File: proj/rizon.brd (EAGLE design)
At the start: 99.1 x 80 mm, 32 parts, among them J1 PWRJACK5521, P1 ADDR, P2 DATA, P3 CTL, P4 PWR, P5 10k, U1 Z8400, U2 AS6C62256PDIP, U3 AS6C62256PDIP, U4 AT28C64BPLCC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

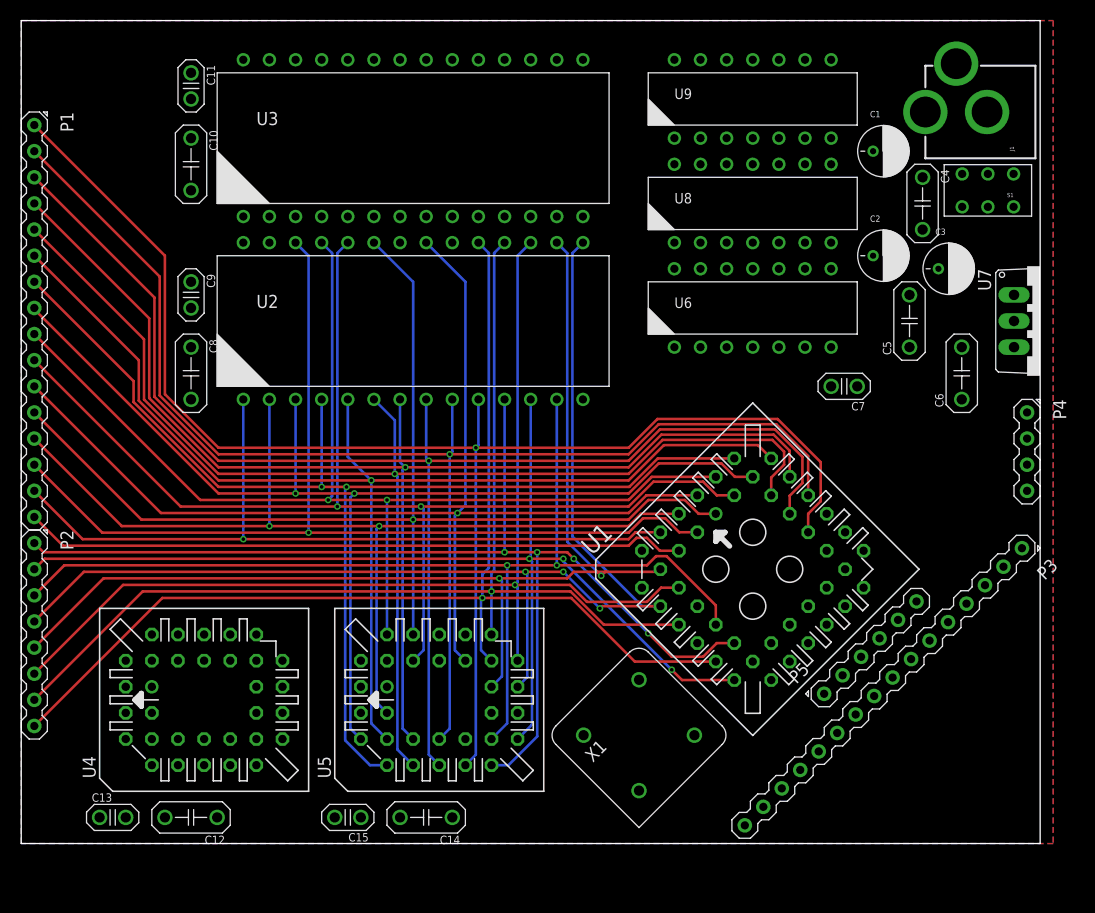
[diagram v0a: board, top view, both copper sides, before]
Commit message: Rizon board routing
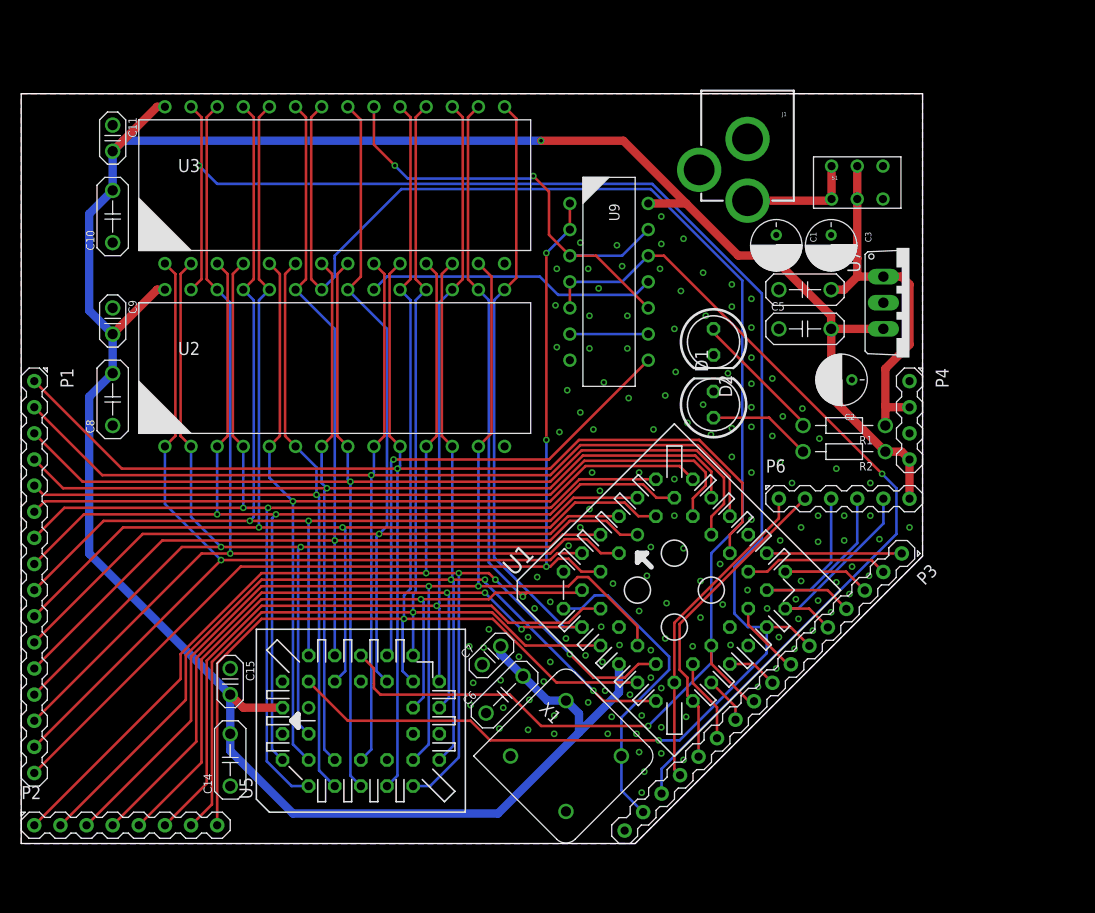
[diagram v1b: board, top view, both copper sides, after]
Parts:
- removed C12: 1uF, dooba:CAP_508
- removed C13: 100nF, dooba:CAP_DISC
- removed P5: 10k, dooba:PIN_6
- removed U4: AT28C64BPLCC, dooba:PLCC-S32--SOCKET
- removed U6, U8: 7432PDIP, dooba:PDIP14
- added D1: VCC, dooba:LED5MM
- added D2: VIN, dooba:LED5MM
- added P6: 10k, dooba:PIN_6
- added R1, R2: 1k, dooba:RES8MM
- moved C6 54.3 mm to (47.0, 14.5), turned to 45 degrees
- moved C7 43.1 mm to (45.7, 18.3), turned to 45 degrees
- moved P1 24.9 mm to (1.27, 25.9)
- moved J1 23.5 mm to (70.6, 68.6), turned to 180 degrees
- moved U9 22.6 mm to (57.1, 54.6), turned to 270 degrees
- moved P2 20.6 mm to (10.2, 1.78), turned to 0 degrees
- moved C14 19.9 mm to (20.3, 8.13), turned to 90 degrees
- moved C15 17.5 mm to (20.3, 15.7), turned to 270 degrees
- moved C4 14.2 mm to (76.2, 53.8), turned to 0 degrees
- moved C1 13.9 mm to (73.4, 58.2), turned to 270 degrees
- moved U7 12.8 mm to (86.4, 52.6)
- moved C2 12.7 mm to (79.8, 45.1), turned to 180 degrees
- moved S1 12.7 mm to (81.3, 64.3), turned to 0 degrees
- moved P4 11.8 mm to (86.4, 41.1)
- moved P3 11.7 mm to (72.1, 14.7)
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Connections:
- removed net !HIGH_ADDR: U8.P$4, U9.P$3
- removed net !MEM_SELECT_LOWRAM: U6.P$6, U8.P$1
- removed net !MEM_SELECT_ROM: U6.P$10, U6.P$13, U6.P$3
- removed net !MEM_SELECT_ROM_BANK0: U6.P$8, U8.P$9
- removed net !MEM_SELECT_ROM_BANK1: U6.P$11, U8.P$12
- removed net !RAM_BANK1_CE: U3.P$20, U8.P$6
- removed net !ROM_BANK0_CE: U4.23, U8.P$8
- removed net !ROM_BANK1: U6.P$12, U9.P$6
- removed net !ROM_BANK1_CE: U5.23, U8.P$11
- new net !ADDR15: U3.P$20, U9.P$10, U9.P$13, U9.P$3
- new net !ROM_CE: U5.23, U9.P$8
- new net N$1: D2.A, R1.P$2
- new net N$2: D1.A, R2.P$2
- net !BUSREQ: now also P3.3, P6.3; no longer P3.2, P5.6
- net !INT: now also P6.2; no longer P5.2
- net !MREQ: no longer U8.P$10, U8.P$13, U8.P$2, U8.P$5
- net !NMI: now also P6.1; no longer P5.3
- net !RAM_BANK0_CE: now also U9.P$11; no longer U8.P$3
- net !RD: no longer U4.25
- net !RESET: now also P3.4, P6.4; no longer P3.3, P5.5
- net !RFSH: now also P3.2; no longer P3.5
- net !ROM_EN: now also U9.P$12, U9.P$4, U9.P$5; no longer U6.P$2, U9.P$10, U9.P$9
- net !WAIT: now also P3.5, P6.5; no longer P3.4, P5.4
- net !WR: no longer U4.31
- net ADDR0: no longer U4.11
- net ADDR1: no longer U4.10
- net ADDR10: no longer U4.24
- net ADDR11: no longer U4.27
- net ADDR12: no longer U4.3
- net ADDR13: no longer U6.P$9, U9.P$4, U9.P$5
- net ADDR15: no longer U6.P$1, U6.P$4
- net ADDR2: no longer U4.9
- net ADDR3: no longer U4.8
- net ADDR4: no longer U4.7
- net ADDR5: no longer U4.6
- net ADDR6: no longer U4.5
- net ADDR7: no longer U4.4
- net ADDR8: no longer U4.29
- net ADDR9: no longer U4.28
- net DATA0: no longer U4.13
- net DATA1: no longer U4.14
- net DATA2: no longer U4.15
- net DATA3: no longer U4.18
- net DATA4: no longer U4.19
- net DATA5: no longer U4.20
- net DATA6: no longer U4.21
- net DATA7: no longer U4.22
- net GND: now also D1.K, D2.K; no longer C12.P$1, C13.P$1, U4.16, U6.P$7, U8.P$7
- net ROM_EN: now also U9.P$6, U9.P$9; no longer U6.P$5, U9.P$8
- net VCC: now also P6.6, R2.P$1; no longer C12.P$2, C13.P$2, P5.1, U4.32, U6.P$14, U8.P$14
- net VIN: now also R1.P$1
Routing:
- net VCC: track 0.00 -> 255.0 mm, vias 0 -> 1
- net !WR: track 0.00 -> 172.5 mm, vias 0 -> 2
- net !RD: track 0.00 -> 154.9 mm, vias 0 -> 1
- net !ROM_EN: track 0.00 -> 83.9 mm, vias 0 -> 1
- net !ADDR15: track 0.00 -> 48.3 mm, vias 0 -> 2
- net !ROM_CE: track 0.00 -> 48.1 mm, vias 0 -> 1
- net VIN: track 0.00 -> 38.9 mm
- net ADDR15: track 64.7 -> 100.4 mm, vias 0 -> 3
- net !NMI: track 0.00 -> 31.3 mm
- net CLK: track 0.00 -> 31.2 mm
- net !INT: track 0.00 -> 30.9 mm
- net !RAM_BANK0_CE: track 0.00 -> 28.5 mm
- net !RESET: track 0.00 -> 23.5 mm
- net !WAIT: track 0.00 -> 20.3 mm
- net DATA0: track 111.5 -> 131.2 mm
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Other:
- board size 99.1 x 80 mm -> 87.6 x 72.9 mm

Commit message: Completed Rizon main board (CPU + RAM + ROM) Added Rizon footprint and device to library
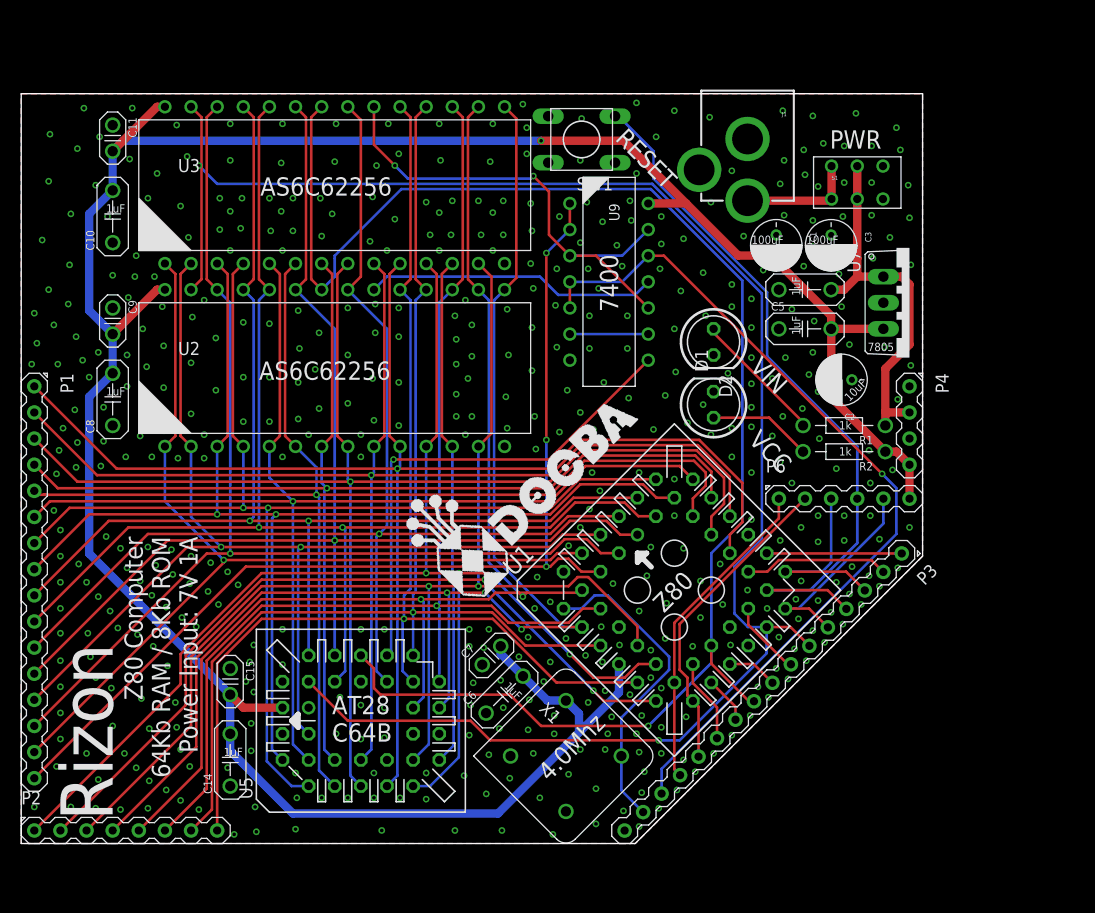
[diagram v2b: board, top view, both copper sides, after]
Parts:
- added SW1: TACTSWTH6MM, dooba:SWITCH_6MM
- moved P1 0.51 mm to (1.27, 25.4)
- moved P4 0.51 mm to (86.4, 40.6)
- moved P2 0.51 mm to (10.2, 1.27)
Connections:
- net !RESET: now also SW1.3
- net GND: now also SW1.1
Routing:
- net !RESET: track 23.5 -> 70.6 mm
- net DATA3: track 129.5 -> 130.0 mm
- net DATA0: track 131.2 -> 131.7 mm
- net DATA7: track 118.8 -> 119.3 mm
- net DATA6: track 112.5 -> 113.0 mm
- net DATA5: track 116.9 -> 117.4 mm
- net DATA4: track 120.8 -> 121.3 mm
- net DATA2: track 121.0 -> 121.5 mm
- net DATA1: track 125.2 -> 125.7 mm
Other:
- board text added: "!BUSACK"
- board text added: "!BUSREQ"
- board text added: "!HALT"
- board text added: "!INT"
- board text added: "!IORQ"
- board text added: "!M1"
- board text added: "!MREQ"
- board text added: "!NMI"
- board text added: "!RD"
- board text added: "!RESET"
- board text added: "!RFSH"
- board text added: "!ROM_EN"
- board text added: "!WAIT"
- board text added: "!WR"
- board text added: "100uF"
- board text added: "10uF"
- board text added: "1k"
- board text added: "1uF"
- board text added: "4.0Mhz"
- board text added: "7400"
- board text added: "7805"
- board text added: "ADDR0"
- board text added: "ADDR15"
- board text added: "AS6C62256"
- board text added: "AT28 C64B"
- board text added: "CLK"
- board text added: "DATA0"
- board text added: "DATA7"
- board text added: "GND"
- board text added: "PWR"
- board text added: "RESET"
- board text added: "Rizon"
- board text added: "VCC"
- board text added: "VIN"
- board text added: "Z80"
- board text added: "Z80 Computer 64Kb RAM / 8Kb ROM Power Input: 7V 1A"

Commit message: Started designing Rizon I/O board schematic
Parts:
- X1: value OSC412.7 -> 4.0Mhz
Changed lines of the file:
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@@
 <?xml version="1.0" encoding="utf-8"?>
 <!DOCTYPE eagle SYSTEM "eagle.dtd">
-<eagle version="8.4.0">
+<eagle version="8.4.1">
 <drawing>
 <settings>
@@
 <param name="dpMaxLengthDifference" value="10mm"/>
 <param name="dpGapFactor" value="2.5"/>
+<param name="checkAngle" value="0"/>
 <param name="checkFont" value="1"/>
 <param name="checkRestrict" value="0"/>
@@
 <element name="U7" library="dooba" package="TO220V" value="7805TO220" x="86.36" y="52.578" rot="R270"/>
 <element name="U9" library="dooba" package="PDIP14" value="7400PDIP" x="57.15" y="54.61" rot="R270"/>
-<element name="X1" library="dooba" package="OSC127" value="OSC412.7" x="52.959" y="8.509" rot="R315"/>
+<element name="X1" library="dooba" package="OSC127" value="4.0Mhz" x="52.959" y="8.509" rot="R315"/>
 <element name="P1" library="dooba" package="PIN_16" value="ADDR" x="1.27" y="25.4" rot="R270"/>
 <element name="P2" library="dooba" package="PIN_8" value="DATA" x="10.16" y="1.27"/>

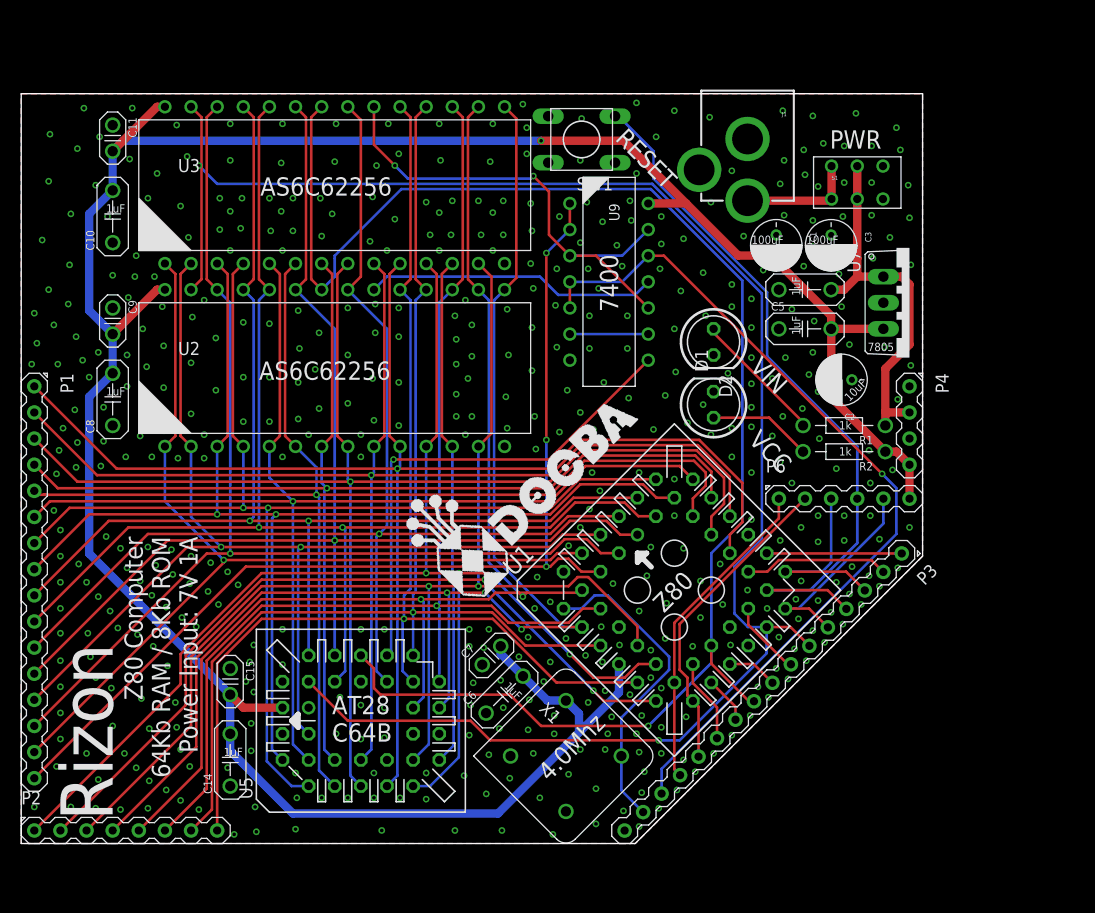
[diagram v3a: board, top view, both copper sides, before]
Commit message: Started SMD version of Rizon Computer Cleaned up library
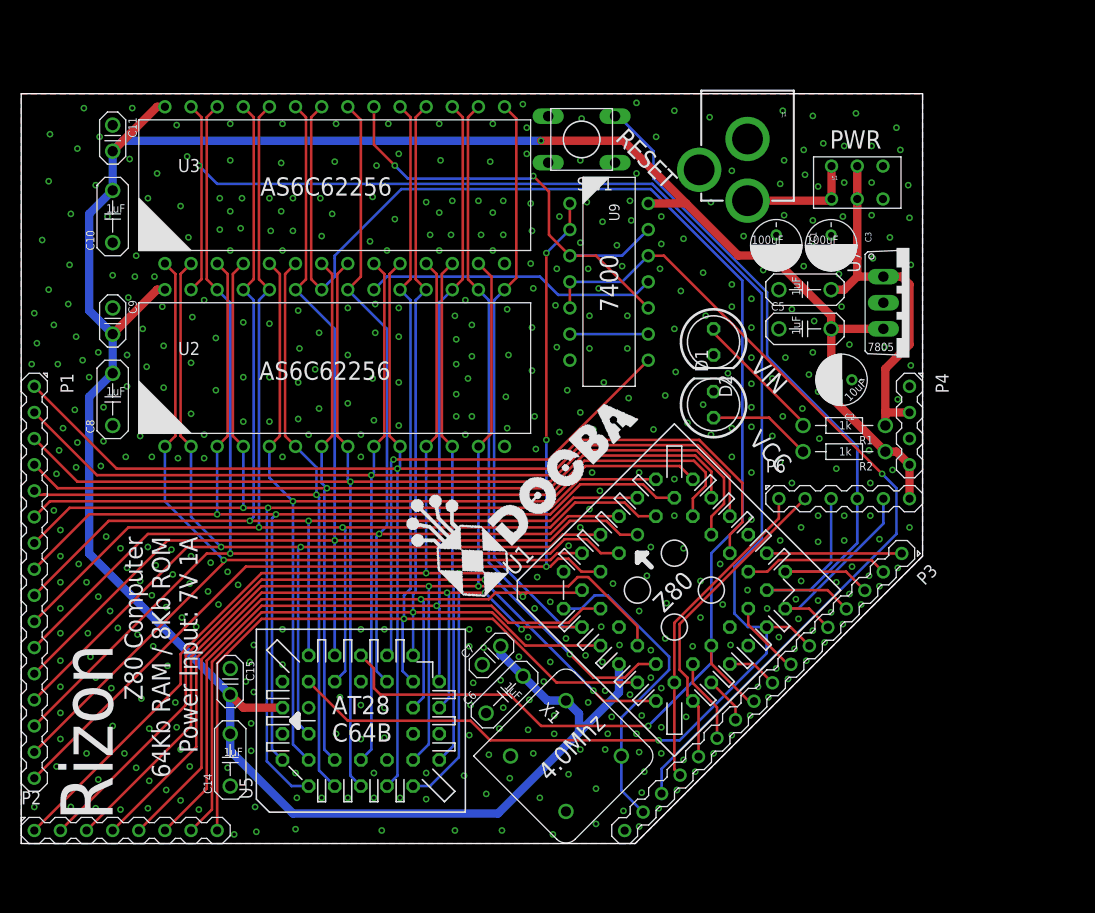
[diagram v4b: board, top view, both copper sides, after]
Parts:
- U1: value Z8400 -> Z8400PLCC
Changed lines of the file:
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@@
 <element name="J1" library="dooba" package="PWRJACK_5521" value="PWRJACK5521" x="70.612" y="68.58" rot="R180"/>
 <element name="S1" library="dooba" package="EG1271" value="SWITCH_SPDT2EG1271" x="81.28" y="64.262"/>
-<element name="U1" library="dooba" package="PLCC-S44-SOCKET" value="Z8400" x="63.5" y="24.638" rot="R45"/>
+<element name="U1" library="dooba" package="PLCC-S44-SOCKET" value="Z8400PLCC" x="63.5" y="24.638" rot="R45"/>
 <element name="U2" library="dooba" package="PDIP28-600" value="AS6C62256PDIP" x="30.48" y="46.228"/>
 <element name="U3" library="dooba" package="PDIP28-600" value="AS6C62256PDIP" x="30.48" y="64.008"/>
